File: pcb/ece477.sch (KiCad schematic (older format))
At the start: 21 parts, among them J1 USB_B, SW1 SW_DIP_x01, U1 ESP32-WROOM-32, U2 FT232RL-REEL, U3 LM3671, U4 ADA254, U5 ADA751

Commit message: added power LED
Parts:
- added D3: LED, LED_SMD:LED_0805_2012Metric, symbol Device:LED
- added R5: 1kΩ, Resistor_SMD:R_0805_2012Metric, symbol Device:R
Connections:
- net GND: now also D3.1 (K)
- net at C3.2, R2.2, SW1.2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: now also R5.1
- new net: D3.2 (A), R5.2
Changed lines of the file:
@@
 $EndComp
-Wire Wire Line
-	3850 2400 4100 2400
 Wire Wire Line
 	5600 4900 4750 4900
@@
 Wire Wire Line
 	5400 2600 5300 2600
-Connection ~ 4100 2900
-Wire Wire Line
-	4100 2900 4100 2400
 $Comp
 L Device:C C3
@@
 Wire Wire Line
 	5850 3100 5850 4250
-Wire Wire Line
-	2650 2000 4450 2000
 Wire Wire Line
 	5100 6500 3900 6500
@@
 Wire Wire Line
 	7750 2000 8050 2000
+Connection ~ 4100 2900
+Connection ~ 4100 2000
+Wire Wire Line
+	4100 2000 4450 2000
+Wire Wire Line
+	2650 2000 4100 2000
+Wire Wire Line
+	3850 2400 3850 2600
+Wire Wire Line
+	3850 2600 4100 2600
+Wire Wire Line
+	4100 2900 4100 2600
+Connection ~ 4100 2600
+Wire Wire Line
+	4100 2000 4100 2200
+$Comp
+L Device:R R5
+U 1 1 5F83C3DE
+P 4100 2450
+F 0 "R5" H 4170 2496 50  0000 L CNN
+F 1 "1kΩ" H 4170 2405 50  0000 L CNN
+F 2 "Resistor_SMD:R_0805_2012Metric" V 4030 2450 50  0001 C CNN
+F 3 "~" H 4100 2450 50  0001 C CNN
+	1    4100 2450
+	-1   0    0    1
+$EndComp
+$Comp
+L Device:LED D3
+U 1 1 5F83C3D8
+P 4100 2150
+F 0 "D3" V 4139 2033 50  0000 R CNN
+F 1 "LED" V 4048 2033 50  0000 R CNN
+F 2 "LED_SMD:LED_0805_2012Metric" H 4100 2150 50  0001 C CNN
+F 3 "~" H 4100 2150 50  0001 C CNN
+	1    4100 2150
+	0    1    1    0
+$EndComp
 $EndSCHEMATC

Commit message: updated pcb
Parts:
- L1: footprint Inductor_SMD:L_0805_2012Metric -> LQH3NPN2R2MMEL:IND_LQH3NPN2R2MMEL
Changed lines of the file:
@@
 F 0 "L1" H 4502 2496 50  0000 L CNN
 F 1 "2.2µH" H 4502 2405 50  0000 L CNN
-F 2 "Inductor_SMD:L_0805_2012Metric" H 4450 2450 50  0001 C CNN
+F 2 "LQH3NPN2R2MMEL:IND_LQH3NPN2R2MMEL" H 4450 2450 50  0001 C CNN
 F 3 "~" H 4450 2450 50  0001 C CNN
 	1    4450 2450

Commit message: updated pcb pinheader width
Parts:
- BT1: footprint Connector_PinHeader_2.00mm:PinHeader_1x02_P2.00mm_Vertical -> Connector_PinHeader_2.54mm:PinHeader_1x02_P2.54mm_Vertical
- U4: footprint Connector_PinSocket_2.00mm:PinSocket_1x08_P2.00mm_Vertical -> Connector_PinSocket_2.54mm:PinSocket_1x08_P2.54mm_Vertical
- U5: footprint Connector_PinHeader_2.00mm:PinHeader_1x05_P2.00mm_Vertical -> Connector_PinHeader_2.54mm:PinHeader_1x05_P2.54mm_Vertical
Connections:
- net GND: now also U1.25 (IO0)
- net at C2.2, L1.1, R1.1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: now also U1.3 (EN)
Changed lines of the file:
@@
 F 0 "BT1" V 2695 2450 50  0000 C CNN
 F 1 "3.7V" V 2786 2450 50  0000 C CNN
-F 2 "Connector_PinHeader_2.00mm:PinHeader_1x02_P2.00mm_Vertical" V 2950 2460 50  0001 C CNN
+F 2 "Connector_PinHeader_2.54mm:PinHeader_1x02_P2.54mm_Vertical" V 2950 2460 50  0001 C CNN
 F 3 "~" V 2950 2460 50  0001 C CNN
 	1    2950 2400
@@
 F 0 "U5" H 6050 6550 50  0000 L CNN
 F 1 "ADA751" H 6050 6450 50  0000 L CNN
-F 2 "Connector_PinHeader_2.00mm:PinHeader_1x05_P2.00mm_Vertical" H 5900 6250 50  0001 C CNN
+F 2 "Connector_PinHeader_2.54mm:PinHeader_1x05_P2.54mm_Vertical" H 5900 6250 50  0001 C CNN
 F 3 "" H 5900 6250 50  0001 C CNN
 	1    5900 6250
@@
 F 0 "U4" H 5900 5925 50  0000 C CNN
 F 1 "ADA254" H 5900 5834 50  0000 C CNN
-F 2 "Connector_PinSocket_2.00mm:PinSocket_1x08_P2.00mm_Vertical" H 5900 5250 50  0001 C CNN
+F 2 "Connector_PinSocket_2.54mm:PinSocket_1x08_P2.54mm_Vertical" H 5900 5250 50  0001 C CNN
 F 3 "" H 5900 5250 50  0001 C CNN
 	1    5900 5250
@@
 	0    1    1    0
 $EndComp
+$Comp
+L power:GND #PWR0104
+U 1 1 5F864B89
+P 4500 3950
+F 0 "#PWR0104" H 4500 3700 50  0001 C CNN
+F 1 "GND" H 4505 3777 50  0000 C CNN
+F 2 "" H 4500 3950 50  0001 C CNN
+F 3 "" H 4500 3950 50  0001 C CNN
+	1    4500 3950
+	1    0    0    -1
+$EndComp
+Wire Wire Line
+	4300 3950 4500 3950
+Wire Wire Line
+	3100 3950 3100 3750
+Wire Wire Line
+	3100 3750 3700 3750
+Connection ~ 3700 3750
 $EndSCHEMATC

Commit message: gui-blink added
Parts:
- R2: value 100kΩ -> 10kΩ
- R3, R4: value 1kΩ -> 500Ω
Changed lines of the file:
@@
 P 5700 2550
 F 0 "R2" H 5770 2596 50  0000 L CNN
-F 1 "100kΩ" H 5770 2505 50  0000 L CNN
+F 1 "10kΩ" H 5770 2505 50  0000 L CNN
 F 2 "Resistor_SMD:R_0805_2012Metric" V 5630 2550 50  0001 C CNN
 F 3 "~" H 5700 2550 50  0001 C CNN
@@
 P 6950 1400
 F 0 "R3" H 7020 1446 50  0000 L CNN
-F 1 "1kΩ" H 7020 1355 50  0000 L CNN
+F 1 "500Ω" H 7020 1355 50  0000 L CNN
 F 2 "Resistor_SMD:R_0805_2012Metric" V 6880 1400 50  0001 C CNN
 F 3 "~" H 6950 1400 50  0001 C CNN
@@
 P 7350 1400
 F 0 "R4" H 7420 1446 50  0000 L CNN
-F 1 "1kΩ" H 7420 1355 50  0000 L CNN
+F 1 "500Ω" H 7420 1355 50  0000 L CNN
 F 2 "Resistor_SMD:R_0805_2012Metric" V 7280 1400 50  0001 C CNN
 F 3 "~" H 7350 1400 50  0001 C CNN

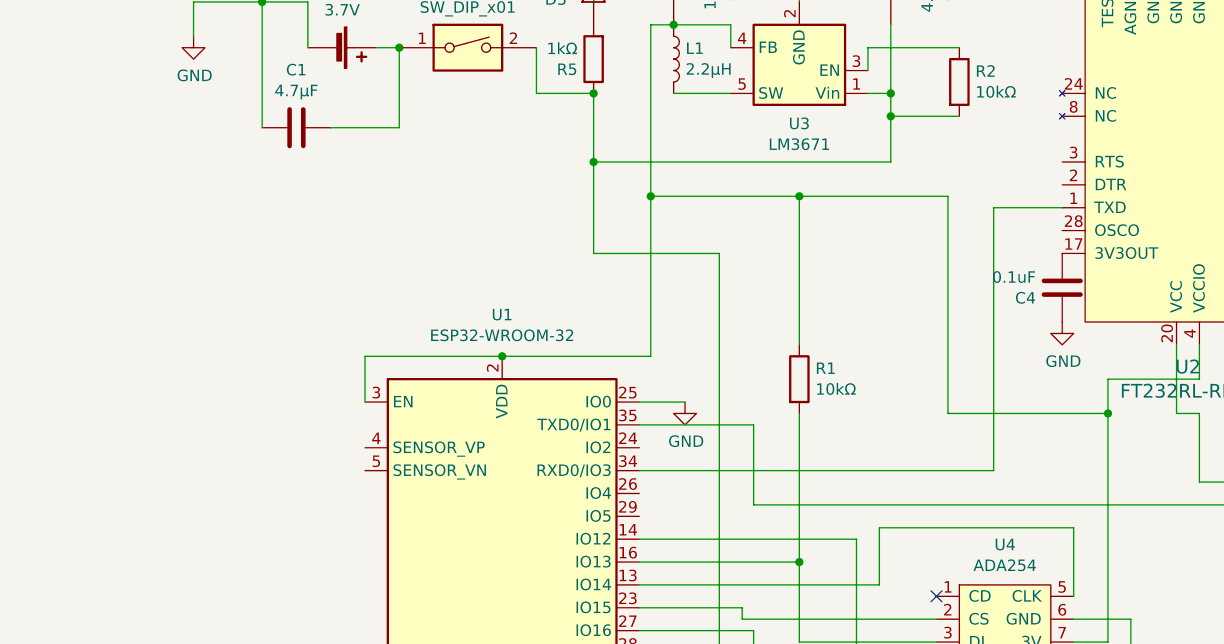
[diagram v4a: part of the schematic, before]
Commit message: updated pcb with programming transistors
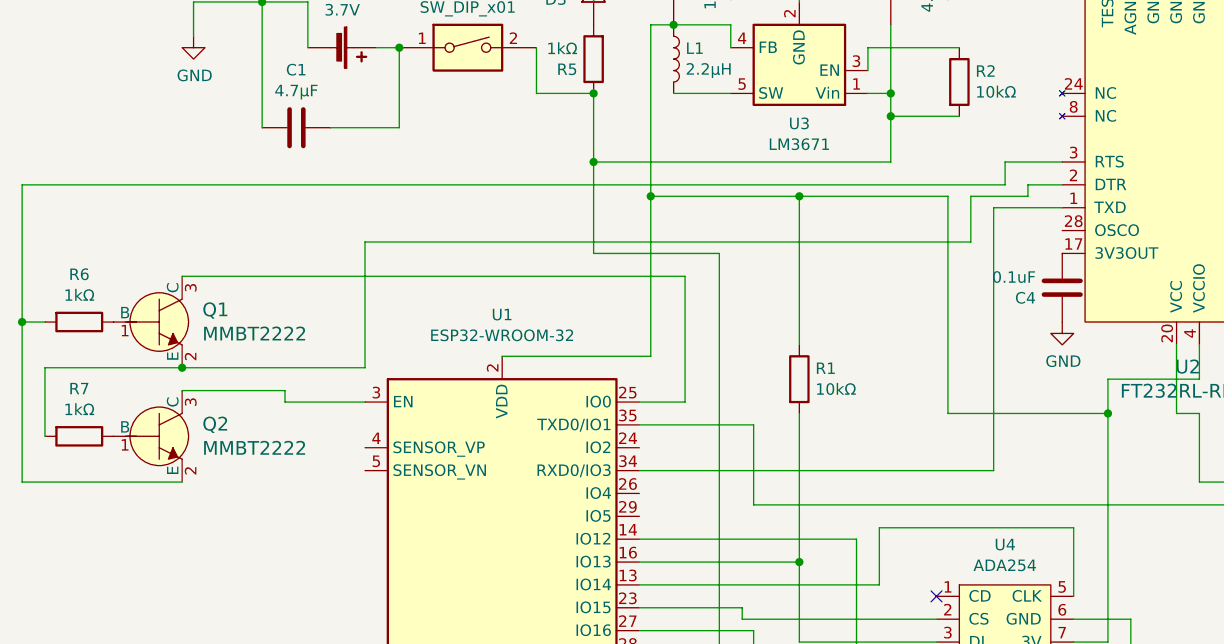
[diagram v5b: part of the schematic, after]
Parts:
- added Q1, Q2: MMBT2222, digikey-footprints:SOT-23-3, symbol dk_Transistors-Bipolar-BJT-Single:MMBT2222A-7-F
- added R6, R7: 1kΩ, Resistor_SMD:R_0805_2012Metric, symbol Device:R
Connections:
- net GND: no longer U1.25 (IO0)
- net at C2.2, L1.1, R1.1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: no longer U1.3 (EN)
- net at U2.2 (DTR): now also Q1.2 (E), R7.2
- net at U2.3 (RTS): now also Q2.2 (E), R6.2
- new net: Q1.3 (C), U1.25 (IO0)
- new net: Q2.3 (C), U1.3 (EN)
- new net: Q1.1 (B), R6.1
- new net: Q2.1 (B), R7.1
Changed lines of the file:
@@
 $EndComp
 $Comp
-L power:GND #PWR0104
-U 1 1 5F864B89
-P 4500 3950
-F 0 "#PWR0104" H 4500 3700 50  0001 C CNN
-F 1 "GND" H 4505 3777 50  0000 C CNN
-F 2 "" H 4500 3950 50  0001 C CNN
-F 3 "" H 4500 3950 50  0001 C CNN
-	1    4500 3950
+L dk_Transistors-Bipolar-BJT-Single:MMBT2222A-7-F Q1
+U 1 1 5F8B6765
+P 2200 3600
+F 0 "Q1" H 2388 3653 60  0000 L CNN
+F 1 "MMBT2222" H 2388 3547 60  0000 L CNN
+F 2 "digikey-footprints:SOT-23-3" H 2400 3800 60  0001 L CNN
+F 3 "https://www.diodes.com/assets/Datasheets/ds30041.pdf" H 2400 3900 60  0001 L CNN
+F 4 "MMBT2222A-FDICT-ND" H 2400 4000 60  0001 L CNN "Digi-Key_PN"
+F 5 "MMBT2222A-7-F" H 2400 4100 60  0001 L CNN "MPN"
+F 6 "Discrete Semiconductor Products" H 2400 4200 60  0001 L CNN "Category"
+F 7 "Transistors - Bipolar (BJT) - Single" H 2400 4300 60  0001 L CNN "Family"
+F 8 "https://www.diodes.com/assets/Datasheets/ds30041.pdf" H 2400 4400 60  0001 L CNN "DK_Datasheet_Link"
+F 9 "/product-detail/en/diodes-incorporated/MMBT2222A-7-F/MMBT2222A-FDICT-ND/815723" H 2400 4500 60  0001 L CNN "DK_Detail_Page"
+F 10 "TRANS NPN 40V 0.6A SMD SOT23-3" H 2400 4600 60  0001 L CNN "Description"
+F 11 "Diodes Incorporated" H 2400 4700 60  0001 L CNN "Manufacturer"
+F 12 "Active" H 2400 4800 60  0001 L CNN "Status"
+	1    2200 3600
 	1    0    0    -1
 $EndComp
+$Comp
+L dk_Transistors-Bipolar-BJT-Single:MMBT2222A-7-F Q2
+U 1 1 5F8C782C
+P 2200 4100
+F 0 "Q2" H 2388 4153 60  0000 L CNN
+F 1 "MMBT2222" H 2388 4047 60  0000 L CNN
+F 2 "digikey-footprints:SOT-23-3" H 2400 4300 60  0001 L CNN
+F 3 "https://www.diodes.com/assets/Datasheets/ds30041.pdf" H 2400 4400 60  0001 L CNN
+F 4 "MMBT2222A-FDICT-ND" H 2400 4500 60  0001 L CNN "Digi-Key_PN"
+F 5 "MMBT2222A-7-F" H 2400 4600 60  0001 L CNN "MPN"
+F 6 "Discrete Semiconductor Products" H 2400 4700 60  0001 L CNN "Category"
+F 7 "Transistors - Bipolar (BJT) - Single" H 2400 4800 60  0001 L CNN "Family"
+F 8 "https://www.diodes.com/assets/Datasheets/ds30041.pdf" H 2400 4900 60  0001 L CNN "DK_Datasheet_Link"
+F 9 "/product-detail/en/diodes-incorporated/MMBT2222A-7-F/MMBT2222A-FDICT-ND/815723" H 2400 5000 60  0001 L CNN "DK_Detail_Page"
+F 10 "TRANS NPN 40V 0.6A SMD SOT23-3" H 2400 5100 60  0001 L CNN "Description"
+F 11 "Diodes Incorporated" H 2400 5200 60  0001 L CNN "Manufacturer"
+F 12 "Active" H 2400 5300 60  0001 L CNN "Status"
+	1    2200 4100
+	1    0    0    -1
+$EndComp
+$Comp
+L Device:R R6
+U 1 1 5F8F8ACB
+P 1850 3600
+F 0 "R6" V 1643 3600 50  0000 C CNN
+F 1 "1kΩ" V 1734 3600 50  0000 C CNN
+F 2 "Resistor_SMD:R_0805_2012Metric" V 1780 3600 50  0001 C CNN
+F 3 "~" H 1850 3600 50  0001 C CNN
+	1    1850 3600
+	0    1    1    0
+$EndComp
+$Comp
+L Device:R R7
+U 1 1 5F8F9118
+P 1850 4100
+F 0 "R7" V 1643 4100 50  0000 C CNN
+F 1 "1kΩ" V 1734 4100 50  0000 C CNN
+F 2 "Resistor_SMD:R_0805_2012Metric" V 1780 4100 50  0001 C CNN
+F 3 "~" H 1850 4100 50  0001 C CNN
+	1    1850 4100
+	0    1    1    0
+$EndComp
 Wire Wire Line
-	4300 3950 4500 3950
+	2300 3800 1700 3800
 Wire Wire Line
-	3100 3950 3100 3750
+	1700 3800 1700 4100
 Wire Wire Line
-	3100 3750 3700 3750
-Connection ~ 3700 3750
+	1700 3600 1600 3600
+Wire Wire Line
+	1600 3600 1600 4300
+Wire Wire Line
+	1600 4300 2300 4300
+Wire Wire Line
+	2300 3400 4500 3400
+Wire Wire Line
+	4500 3400 4500 3950
+Wire Wire Line
+	4500 3950 4300 3950
+Wire Wire Line
+	1600 3600 1600 3000
+Wire Wire Line
+	1600 3000 5900 3000
+Wire Wire Line
+	5900 3000 5900 2900
+Wire Wire Line
+	5900 2900 6150 2900
+Connection ~ 1600 3600
+Wire Wire Line
+	2300 3900 2750 3900
+Wire Wire Line
+	2750 3900 2750 3950
+Wire Wire Line
+	2750 3950 3100 3950
+Wire Wire Line
+	2300 3800 3100 3800
+Wire Wire Line
+	3100 3800 3100 3250
+Wire Wire Line
+	3100 3250 5750 3250
+Wire Wire Line
+	5750 3250 5750 3050
+Wire Wire Line
+	5750 3050 6000 3050
+Wire Wire Line
+	6000 3050 6000 3000
+Connection ~ 2300 3800
+Wire Wire Line
+	6000 3000 6150 3000
 $EndSCHEMATC
